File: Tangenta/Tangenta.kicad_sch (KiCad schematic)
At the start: 9 parts

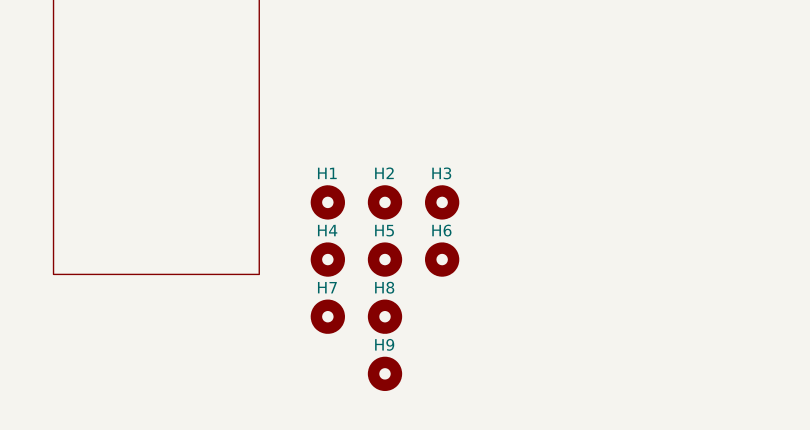
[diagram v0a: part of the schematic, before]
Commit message: Connecting a mounting hole to GND.
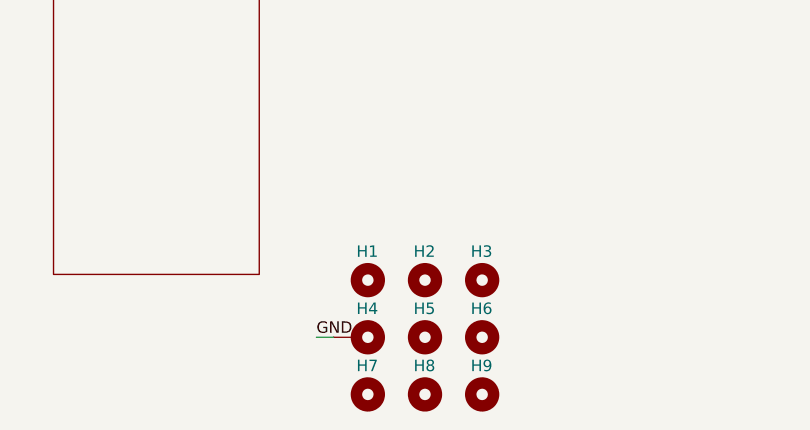
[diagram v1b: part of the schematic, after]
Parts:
- removed H4: MountingHole, MountingHole:MountingHole_4mm_Pad_Via, symbol Mechanical:MountingHole
- added H4: MountingHole_Pad, MountingHole:MountingHole_4mm_Pad_Via, symbol Mechanical:MountingHole_Pad
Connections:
- net GND: now also H4.1
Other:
- moved on the sheet: H1, H2, H3, H5, H6, H7, H8, H9

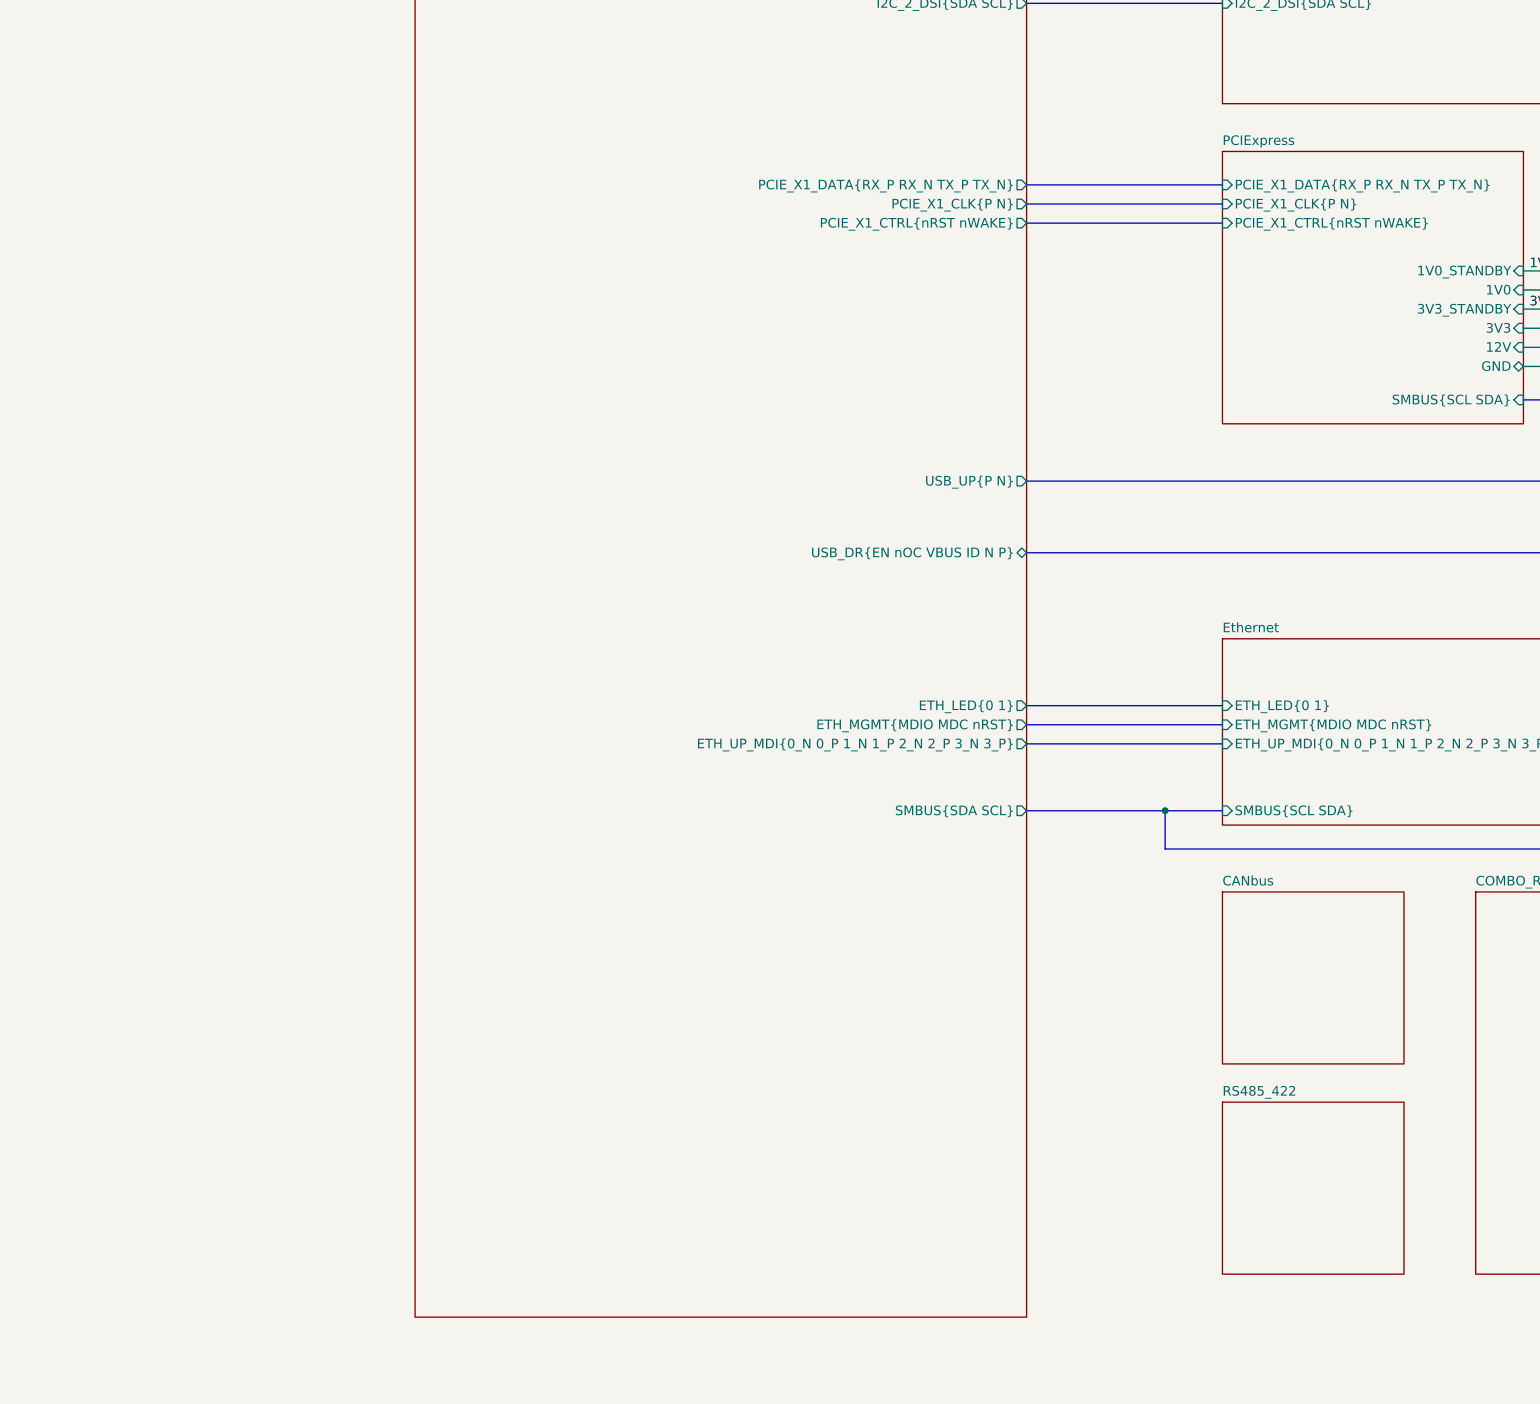
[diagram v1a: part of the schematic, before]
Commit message: UARTs schematic fanout.
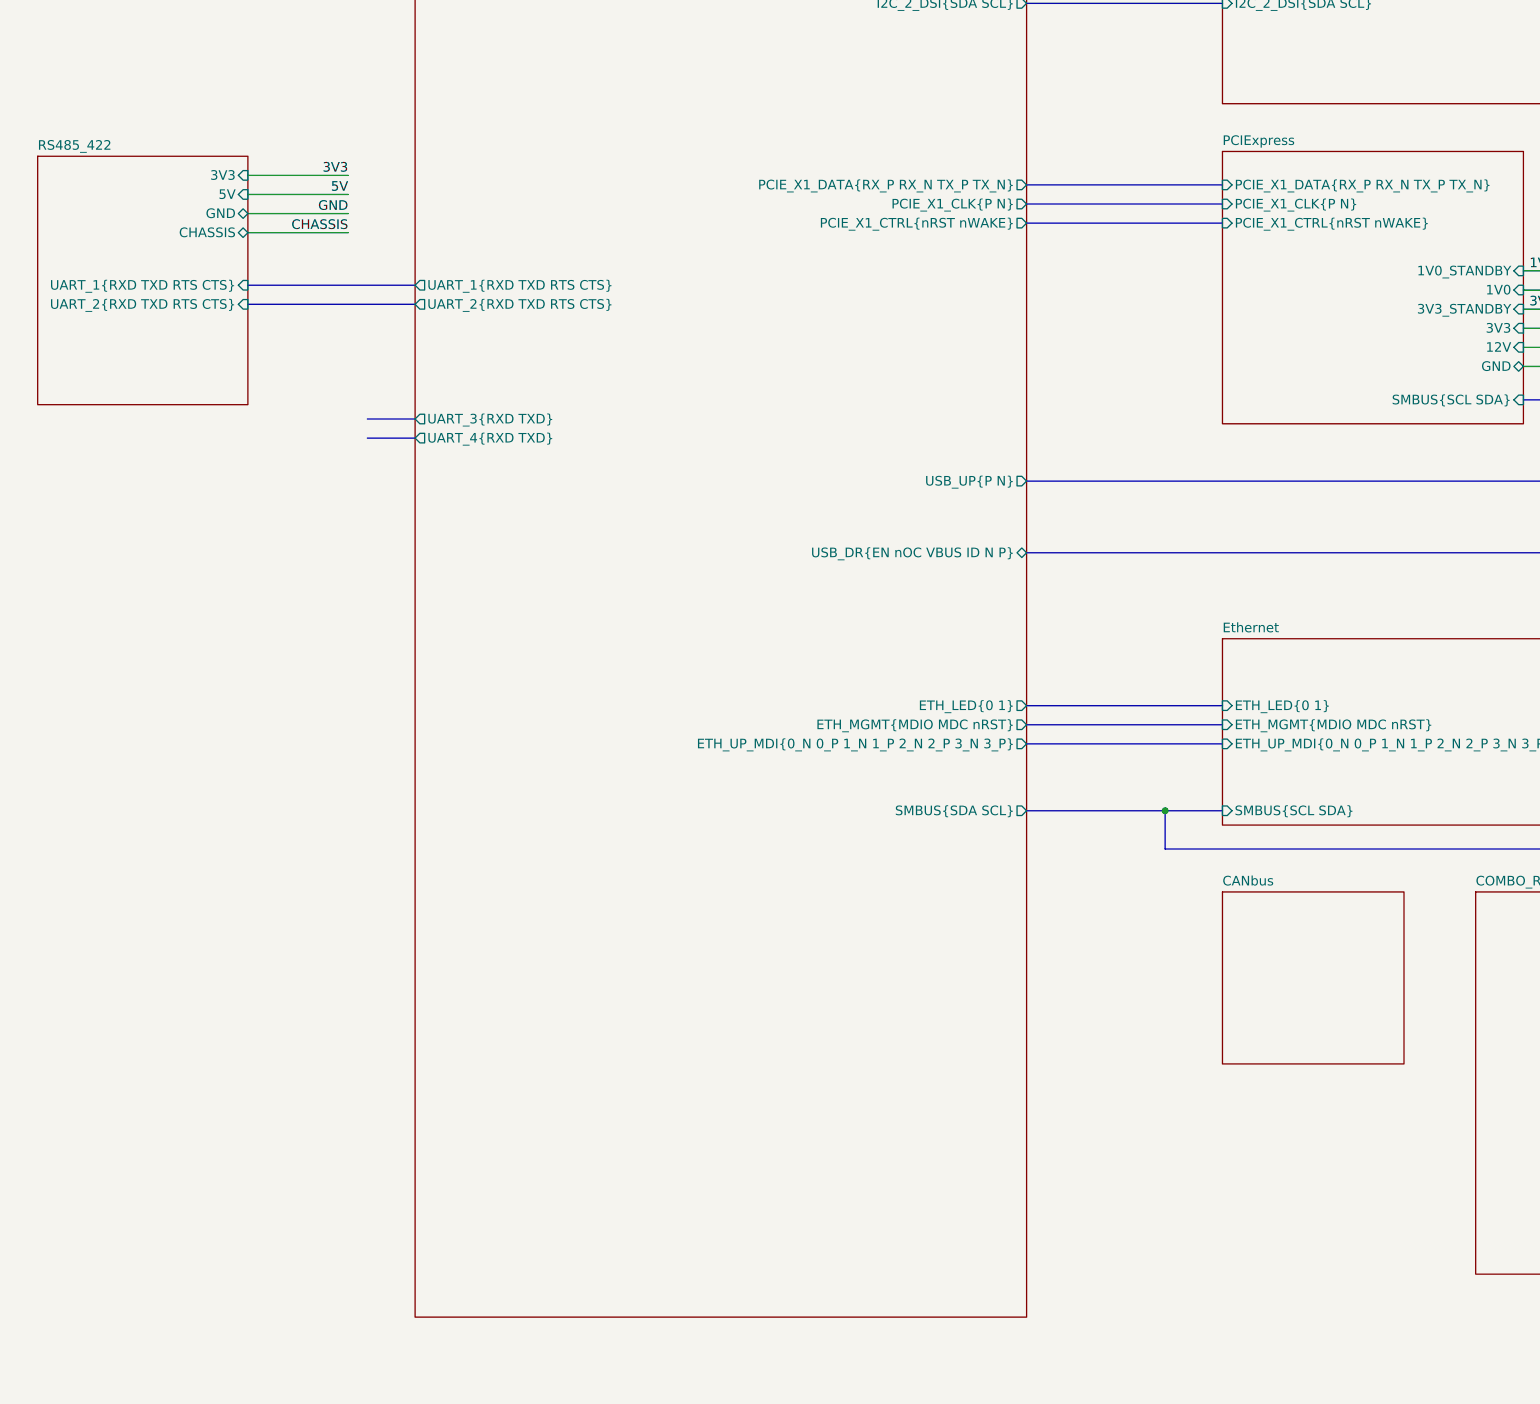
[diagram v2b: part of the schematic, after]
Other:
- sheet RS485_422 ports: added 3V3, 5V, CHASSIS, GND, UART_1{RXD TXD RTS CTS}, UART_2{RXD TXD RTS CTS}; removed none
- sheet Toradex ports: added UART_1{RXD TXD RTS CTS}, UART_2{RXD TXD RTS CTS}, UART_3{RXD TXD}, UART_4{RXD TXD}; removed none
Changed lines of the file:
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@@
+    (stroke (width 0) (type default))
+  )
+  (bus (pts (xy 85.09 137.795) (xy 107.315 137.795))
     (stroke (width 0) (type default))
   )
@@
     (stroke (width 0) (type default))
   )
+  (wire (pts (xy 85.09 125.73) (xy 98.425 125.73))
+    (stroke (width 0) (type default))
+  )
   (wire (pts (xy 389.255 31.75) (xy 402.59 31.75))
     (stroke (width 0) (type default))
   )
+  (wire (pts (xy 85.09 128.27) (xy 98.425 128.27))
+    (stroke (width 0) (type default))
+  )
   (wire (pts (xy 107.315 24.765) (xy 93.98 24.765))
     (stroke (width 0) (type default))
@@
     (stroke (width 0) (type default))
   )
+  (bus (pts (xy 100.965 155.575) (xy 107.315 155.575))
+    (stroke (width 0) (type default))
+  )
   (wire (pts (xy 294.64 107.315) (xy 307.975 107.315))
     (stroke (width 0) (type default))
@@
     (stroke (width 0) (type default))
   )
+  (wire (pts (xy 85.09 120.65) (xy 98.425 120.65))
+    (stroke (width 0) (type default))
+  )
   (wire (pts (xy 389.255 24.13) (xy 402.59 24.13))
     (stroke (width 0) (type default))
@@
     (stroke (width 0) (type default))
   )
+  (bus (pts (xy 85.09 135.255) (xy 107.315 135.255))
+    (stroke (width 0) (type default))
+  )
   (bus (pts (xy 188.595 196.215) (xy 214.63 196.215))
     (stroke (width 0) (type default))
@@
     (stroke (width 0) (type default))
   )
+  (wire (pts (xy 85.09 123.19) (xy 98.425 123.19))
+    (stroke (width 0) (type default))
+  )
   (bus (pts (xy 188.595 124.46) (xy 214.63 124.46))
     (stroke (width 0) (type default))
@@
   )
   (bus (pts (xy 278.765 125.73) (xy 278.765 150.495))
+    (stroke (width 0) (type default))
+  )
+  (bus (pts (xy 100.965 153.035) (xy 107.315 153.035))
     (stroke (width 0) (type default))
   )
@@
     (effects (font (size 1.27 1.27)) (justify right bottom))
   )
+  (label "3V3" (at 98.425 120.65 180) (fields_autoplaced)
+    (effects (font (size 1.27 1.27)) (justify right bottom))
+  )
   (label "GND" (at 277.495 273.685 0) (fields_autoplaced)
     (effects (font (size 1.27 1.27)) (justify left bottom))
@@
     (effects (font (size 1.27 1.27)) (justify left bottom))
   )
+  (label "GND" (at 98.425 125.73 180) (fields_autoplaced)
+    (effects (font (size 1.27 1.27)) (justify right bottom))
+  )
   (label "GND" (at 402.59 52.07 180) (fields_autoplaced)
     (effects (font (size 1.27 1.27)) (justify right bottom))
@@
   )
   (label "1V1" (at 402.59 49.53 180) (fields_autoplaced)
+    (effects (font (size 1.27 1.27)) (justify right bottom))
+  )
+  (label "CHASSIS" (at 98.425 128.27 180) (fields_autoplaced)
+    (effects (font (size 1.27 1.27)) (justify right bottom))
+  )
+  (label "5V" (at 98.425 123.19 180) (fields_autoplaced)
     (effects (font (size 1.27 1.27)) (justify right bottom))
   )
@@
     )
   )
-  (sheet (at 214.63 243.84) (size 24.13 22.86) (fields_autoplaced)
-    (stroke (width 0.1524) (type solid))
-    (fill (color 0 0 0 0.0000))
-    (property "Sheetname" "RS485_422" (at 214.63 243.1284 0)
-      (effects (font (size 1.27 1.27)) (justify left bottom))
-    )
-    (property "Sheetfile" "RS485_422.kicad_sch" (at 214.63 267.9196 0)
-      (effects (font (size 1.27 1.27)) (justify left top) hide)
+  (sheet (at 57.15 118.11) (size 27.94 33.02) (fields_autoplaced)
+    (stroke (width 0.1524) (type solid))
+    (fill (color 0 0 0 0.0000))
+    (property "Sheetname" "RS485_422" (at 57.15 117.3984 0)
+      (effects (font (size 1.27 1.27)) (justify left bottom))
+    )
+    (property "Sheetfile" "RS485_422.kicad_sch" (at 57.15 151.7146 0)
+      (effects (font (size 1.27 1.27)) (justify left top) hide)
+    )
+    (pin "GND" bidirectional (at 85.09 125.73 0)
+      (effects (font (size 1.27 1.27)) (justify right))
+    )
+    (pin "5V" input (at 85.09 123.19 0)
+      (effects (font (size 1.27 1.27)) (justify right))
+    )
+    (pin "CHASSIS" bidirectional (at 85.09 128.27 0)
+      (effects (font (size 1.27 1.27)) (justify right))
+    )
+    (pin "3V3" input (at 85.09 120.65 0)
+      (effects (font (size 1.27 1.27)) (justify right))
+    )
+    (pin "UART_1{RXD TXD RTS CTS}" input (at 85.09 135.255 0)
+      (effects (font (size 1.27 1.27)) (justify right))
+    )
+    (pin "UART_2{RXD TXD RTS CTS}" input (at 85.09 137.795 0)
+      (effects (font (size 1.27 1.27)) (justify right))
     )
     (instances
@@
       (effects (font (size 1.27 1.27)) (justify right))
     )
-    (instances
+    (pin "UART_4{RXD TXD}" output (at 107.315 155.575 180)
+      (effects (font (size 1.27 1.27)) (justify left))
+    )
+    (pin "UART_1{RXD TXD RTS CTS}" output (at 107.315 135.255 180)
+      (effects (font (size 1.27 1.27)) (justify left))
+    )
+    (pin "UART_2{RXD TXD RTS CTS}" output (at 107.315 137.795 180)
+      (effects (font (size 1.27 1.27)) (justify left))
+    )
+    (pin "UART_3{RXD TXD}" output (at 107.315 153.035 180)
+      (effects (font (size 1.27 1.27)) (justify left))
+    )
+    (instances

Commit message: ...
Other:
- sheet RS485_422 ports: added 1V8, RS485_CH_1{A B}, RS485_CH_2{A B}; removed 3V3
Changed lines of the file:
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@@
     (effects (font (size 1.27 1.27)) (justify right bottom))
   )
-  (label "3V3" (at 98.425 120.65 180) (fields_autoplaced)
+  (label "1V8" (at 98.425 120.65 180) (fields_autoplaced)
     (effects (font (size 1.27 1.27)) (justify right bottom))
   )
@@
       (effects (font (size 1.27 1.27)) (justify right))
     )
-    (pin "3V3" input (at 85.09 120.65 0)
-      (effects (font (size 1.27 1.27)) (justify right))
-    )
     (pin "UART_1{RXD TXD RTS CTS}" input (at 85.09 135.255 0)
       (effects (font (size 1.27 1.27)) (justify right))
@@
       (effects (font (size 1.27 1.27)) (justify right))
     )
-    (instances
+    (pin "1V8" input (at 85.09 120.65 0)
+      (effects (font (size 1.27 1.27)) (justify right))
+    )
+    (pin "RS485_CH_1{A B}" output (at 57.15 142.875 180)
+      (effects (font (size 1.27 1.27)) (justify left))
+    )
+    (pin "RS485_CH_2{A B}" output (at 57.15 145.415 180)
+      (effects (font (size 1.27 1.27)) (justify left))
+    )
+    (instances

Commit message: RS485 current progress...
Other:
- note added: "GPIOs/IOs FANs Reset/Power pins and buttons"
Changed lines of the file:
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@@
     (stroke (width 0) (type default))
+  )
+  (text "GPIOs/IOs\n\nFANs\n\nReset/Power pins\nand buttons" (at 28.575 75.565 0)
+    (effects (font (size 5 5)) (justify left bottom))
   )
   (label "CHASSIS" (at 307.975 107.315 180) (fields_autoplaced)

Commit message: ...
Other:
- note added: "GPIOs/IOs FANs Reset/Power pins and buttons CR2032 Battery"
- note removed: "GPIOs/IOs FANs Reset/Power pins and buttons"
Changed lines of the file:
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@@
     (stroke (width 0) (type default))
   )
-  (text "GPIOs/IOs\n\nFANs\n\nReset/Power pins\nand buttons" (at 28.575 75.565 0)
+  (text "GPIOs/IOs\n\nFANs\n\nReset/Power pins\nand buttons\n\nCR2032 Battery"
+    (at 28.575 91.44 0)
     (effects (font (size 5 5)) (justify left bottom))
   )

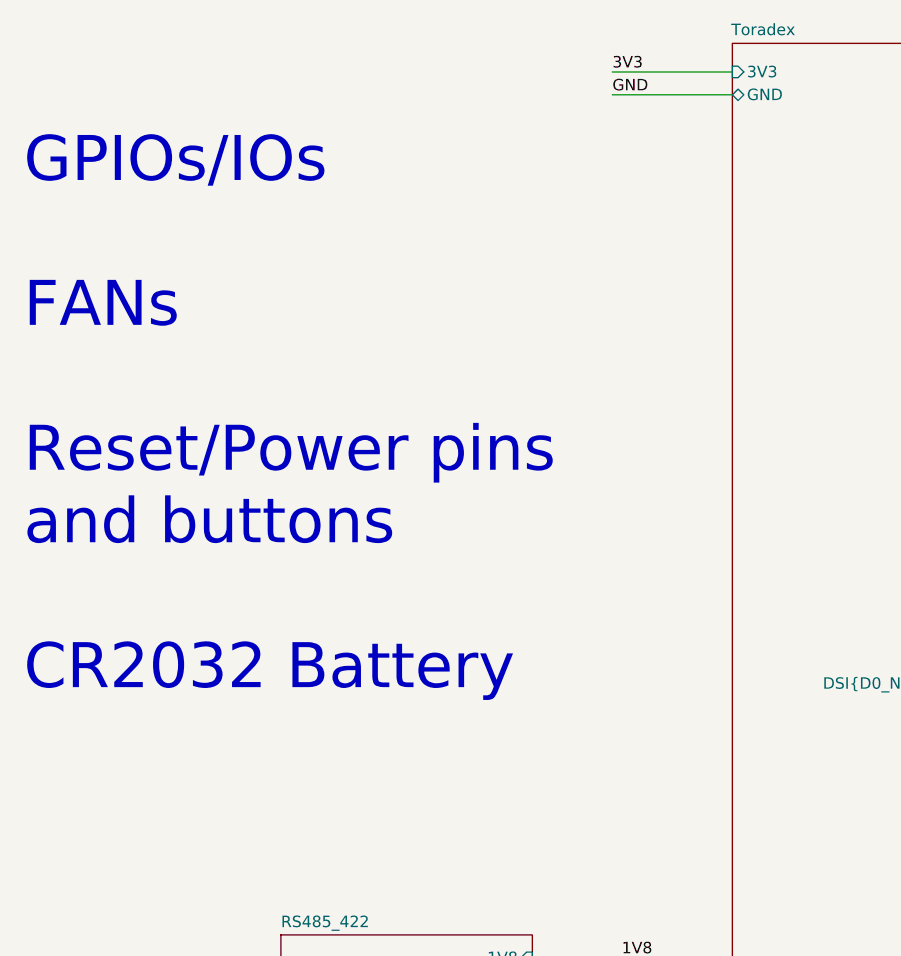
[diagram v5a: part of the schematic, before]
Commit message: Level shifters, continued...
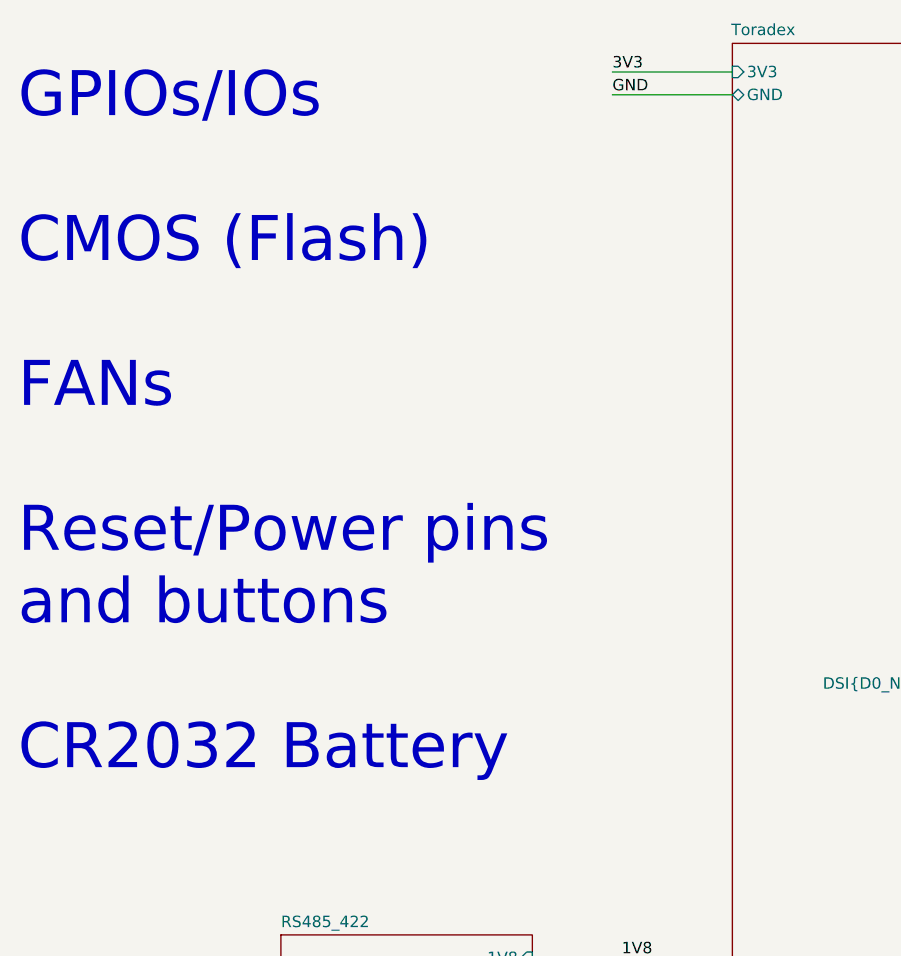
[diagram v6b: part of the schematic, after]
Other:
- note added: "GPIOs/IOs CMOS (Flash) FANs Reset/Power pins and buttons CR2032 Battery"
- note removed: "GPIOs/IOs FANs Reset/Power pins and buttons CR2032 Battery"
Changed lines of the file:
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@@
     (stroke (width 0) (type default))
   )
-  (text "GPIOs/IOs\n\nFANs\n\nReset/Power pins\nand buttons\n\nCR2032 Battery"
-    (at 28.575 91.44 0)
+  (text "GPIOs/IOs\n\nCMOS (Flash)\n\nFANs\n\nReset/Power pins\nand buttons\n\nCR2032 Battery"
+    (at 27.94 100.33 0)
     (effects (font (size 5 5)) (justify left bottom))
   )
